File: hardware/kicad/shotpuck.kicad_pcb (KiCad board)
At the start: 2 copper layers, 36 x 34.8 mm, 34 parts, among them J1 Samzo PR5L4015-2P-C-F, J2 SWD pads, Q1 DMN63D8LDW, Q2 DMN2004DWK, U1 BMD-340-A-R, U2 LSM6DSO32TR, U3 MCP73831T-2ACI/OT, U4 BQ29700DSER

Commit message: Refine ShotPuck design with updated component specifications and enhanced documentation
- Updated `README.md` to clarify new component specifications and assembly instructions.
- Revised `VALIDATION.md` to include updated performance metrics and validation steps.
- Adjusted `design.py` to reflect changes in component layout and configurations.
- Enhanced `gen_bom.py` and `gen_jlc.py` to ensure accurate sourcing of components.
- Improved `layout.json` to accommodate new design parameters and dimensions.

Co-Authored-By: Claude Opus 5.5 <noreply@anthropic.com>
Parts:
- moved J2 1.12 mm to (-1.70, -13.5)
- moved U1 1.12 mm to (0.00, -11.0)
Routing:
- net GND: track 131.6 -> 66.2 mm, vias 37 -> 35
- net CHG_INH: track 16.4 -> 20.3 mm
- net VBAT: track 39.4 -> 36.0 mm
- net VIN: track 68.4 -> 70.1 mm
- net SCL: track 4.75 -> 3.54 mm
- net ACC_INT1: track 6.94 -> 5.75 mm
- net SDA: track 4.36 -> 3.34 mm
- net VBUS_SNS: track 10.1 -> 11.0 mm
- net VDD: track 24.0 -> 23.2 mm
- net LED_IO: track 1.68 -> 2.29 mm

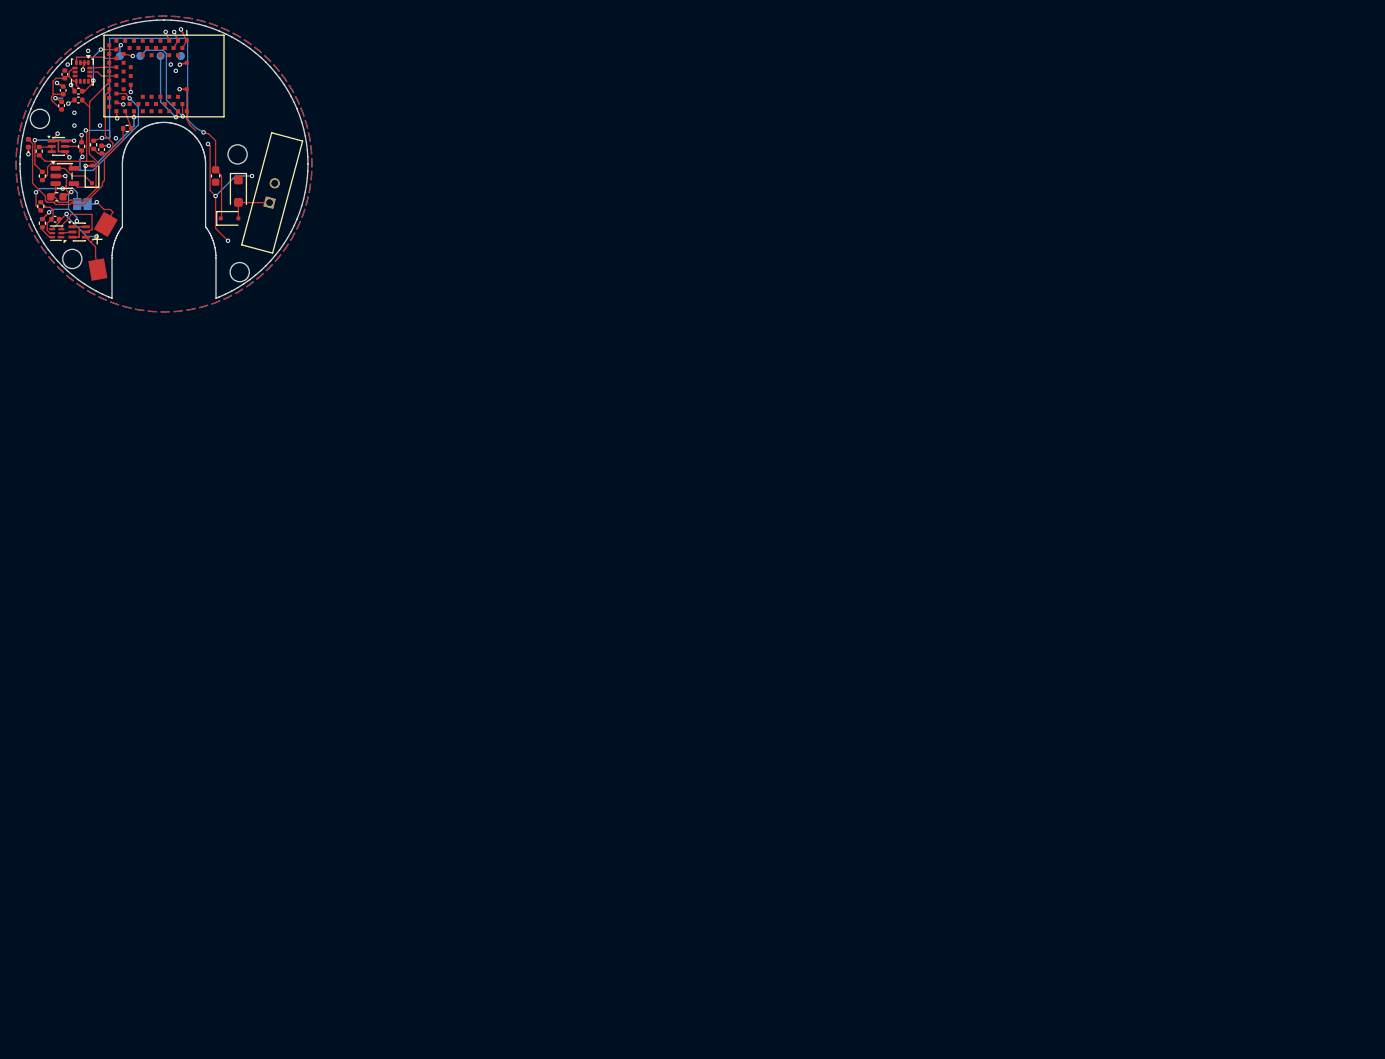
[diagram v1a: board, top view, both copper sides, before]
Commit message: Add USB-C side-port board variant
- J1: side-mounted HRO TYPE-C-31-M-17 (6-pin, power only) replaces the
  magnetic Samzo connector; R10/R11 5.1k pull CC1/CC2 down. Footprint copy
  ShotPuck:..._NoFrontSilk drops the silkscreen outside the board edge.
- Module slid 45 deg around the sleeve; copper-free right side
  (board_shape.rf_keepout), IMU and its caps moved next to the module.
- Decoupling: C5 removed from board and schematic (the BMD-340 has 4.7 uF
  on VCC inside, C4 stays); C6/C7 moved next to IMU pins 8 and 5, C1 next
  to the charger input, vias moved out of U3's pads.
- BT1 uses ShotPuck:LIR1254_Contacts_Edit (pad 2 at 270 deg).
- Schematic: local power symbol ShotPuck:GND_LOCAL keeps the net /GND.
- DRC with zone refill: 0 errors, 0 unconnected, schematic parity clean.

design.py, gen_sch.py and gen_pcb.py still list C5, and gen_sch.py
rewrites ShotPuck.kicad_sym without GND_LOCAL: regenerating undoes the
hand edits.

Co-Authored-By: Claude Opus 5.5 <noreply@anthropic.com>
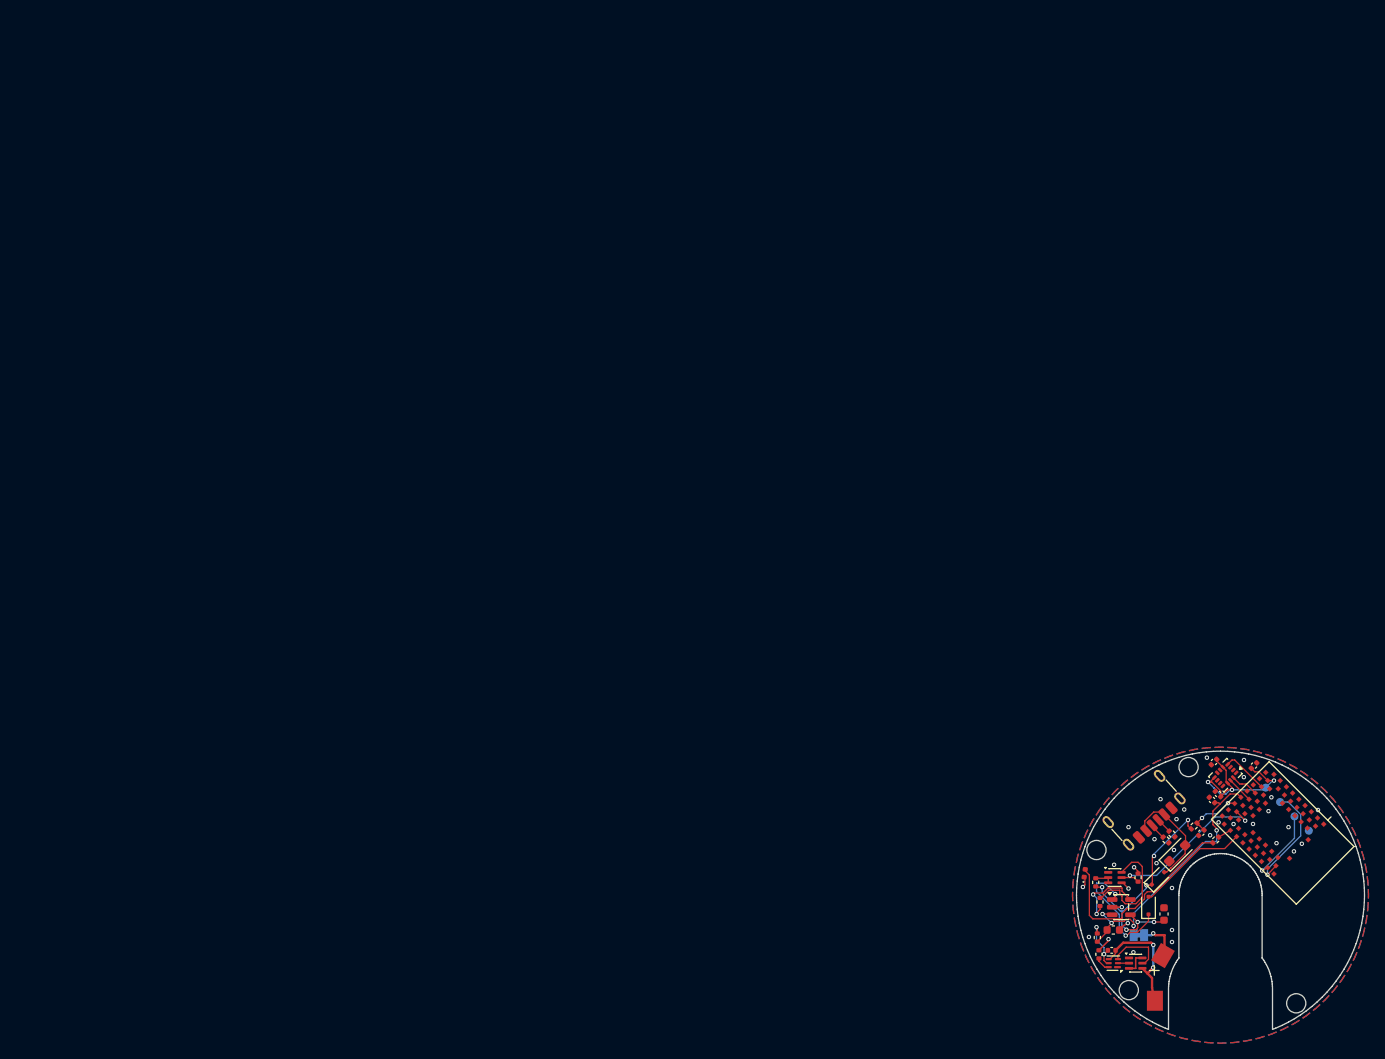
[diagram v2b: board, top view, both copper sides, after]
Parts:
- removed C5: 100n, Capacitor_SMD:C_0402_1005Metric
- added R10: 5.1k 1%, Resistor_SMD:R_0402_1005Metric, F.Cu at (126.0, 83.8)
- added R11: 5.1k 1%, Resistor_SMD:R_0402_1005Metric, F.Cu at (125.2, 84.5)
- BT1: footprint ShotPuck:LIR1254_Contacts -> ShotPuck:LIR1254_Contacts_Edit
- J1: value Samzo PR5L4015-2P-C-F -> TYPE-C-31-M-17; footprint ShotPuck:MagPogo_Samzo_2P -> ShotPuck:USB_C_Receptacle_HRO_TYPE-C-31-M-17_NoFrontSilk
- moved J2 170.5 mm to (140.4, 80.6), turned to -45 degrees
- moved C4 170.4 mm to (136.2, 75.2), turned to 45 degrees
- moved C6 169.9 mm to (131.8, 78.8), turned to 135 degrees
- moved U1 168.8 mm to (139.8, 83.6), turned to 135 degrees
- moved U2 167.7 mm to (132.7, 76.4), turned to -135 degrees
- moved C7 166.6 mm to (131.2, 74.8), turned to -135 degrees
- moved C3 166.5 mm to (131.0, 79.5), turned to 135 degrees
- moved R4 162.6 mm to (131.5, 84.5), turned to -135 degrees
- moved C9 161.8 mm to (129.7, 83.6), turned to -135 degrees
- moved R9 161.8 mm to (128.8, 82.8), turned to 45 degrees
- moved C2 160.7 mm to (118.7, 95.8)
- moved BT1 160.7 mm to (132.1, 103.1)
- moved H2 160.6 mm to (116.6, 85.8)
- moved Q2 160.6 mm to (121.5, 99.9)
- moved R3 160.6 mm to (121.8, 89.2)
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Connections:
- net ACC_INT1 renamed /ACC_INT1
- net BAT_N renamed /BAT_N
- net BAT_P renamed /BAT_P
- net CHG_INH renamed /CHG_INH
- net CHG_STAT renamed /CHG_STAT
- net LED_A renamed /LED_A
- net LED_IO renamed /LED_IO
- net PCM_BAT renamed /PCM_BAT
- net PCM_COUT renamed /PCM_COUT
- net PCM_D renamed /PCM_D
- net PCM_DOUT renamed /PCM_DOUT
- net PCM_VM renamed /PCM_VM
- net PROG renamed /PROG
- net PROG_SW renamed /PROG_SW
- net Q1_GATE renamed /Q1_GATE
- net SCL renamed /SCL
- net SDA renamed /SDA
- net STAT renamed /STAT
- net SWDCLK renamed /SWDCLK
- net SWDIO renamed /SWDIO
- net VBAT renamed /VBAT
- net VBUS_SNS renamed /VBUS_SNS
- net VDD renamed /VDD
- net VIN renamed /VIN
- C1 pad 2: GND -> /GND
- C2 pad 2: GND -> /GND
- C3 pad 2: GND -> /GND
- C4 pad 2: GND -> /GND
- C6 pad 2: GND -> /GND
- C7 pad 2: GND -> /GND
- C9 pad 2: GND -> /GND
- D1 pad 2: VIN_RAW -> /VIN_RAW
- D3 pad 1: GND -> /GND
- D3 pad 2: VIN_RAW -> /VIN_RAW
- D4 pad 1: GND -> /GND
- J2 pad 4: GND -> /GND
- Q1 pad 1: GND -> /GND
- Q1 pad 4: GND -> /GND
- Q2 pad 1: GND -> /GND
- R3 pad 2: GND -> /GND
- R8 pad 2: GND -> /GND
- U1 pad 1: GND -> /GND
- U1 pad 10: (no net) -> unconnected-(U1-P0.29-Pad10)
- U1 pad 11: (no net) -> unconnected-(U1-P0.30-Pad11)
- U1 pad 12: (no net) -> unconnected-(U1-P0.31-Pad12)
- U1 pad 13: (no net) -> unconnected-(U1-P0.00-Pad13)
- U1 pad 14: (no net) -> unconnected-(U1-P0.01-Pad14)
- U1 pad 15: (no net) -> unconnected-(U1-P0.02-Pad15)
- U1 pad 16: GND -> /GND
- U1 pad 18: GND -> /GND
- U1 pad 2: GND -> /GND
- U1 pad 20: (no net) -> unconnected-(U1-P0.04-Pad20)
- U1 pad 22: (no net) -> unconnected-(U1-P0.06-Pad22)
- U1 pad 24: (no net) -> unconnected-(U1-P0.08-Pad24)
- U1 pad 25: (no net) -> unconnected-(U1-P0.09-Pad25)
- U1 pad 26: (no net) -> unconnected-(U1-P0.10-Pad26)
- U1 pad 28: (no net) -> unconnected-(U1-P0.12-Pad28)
- U1 pad 29: GND -> /GND
- U1 pad 3: GND -> /GND
- U1 pad 30: GND -> /GND
- U1 pad 32: (no net) -> unconnected-(U1-P0.14-Pad32)
- U1 pad 34: (no net) -> unconnected-(U1-P0.16-Pad34)
- U1 pad 35: (no net) -> unconnected-(U1-P0.17-Pad35)
- U1 pad 36: (no net) -> unconnected-(U1-P0.21-Pad36)
- U1 pad 37: (no net) -> unconnected-(U1-P0.19-Pad37)
- U1 pad 38: (no net) -> unconnected-(U1-P0.20-Pad38)
- U1 pad 39: (no net) -> unconnected-(U1-P0.18-Pad39)
- U1 pad 4: GND -> /GND
- U1 pad 40: (no net) -> unconnected-(U1-P0.22-Pad40)
- U1 pad 41: (no net) -> unconnected-(U1-P0.23-Pad41)
- U1 pad 42: (no net) -> unconnected-(U1-P0.24-Pad42)
- U1 pad 45: GND -> /GND
- U1 pad 46: GND -> /GND
- U1 pad 47: GND -> /GND
- U1 pad 48: (no net) -> unconnected-(U1-P1.05-Pad48)
- U1 pad 49: (no net) -> unconnected-(U1-P1.06-Pad49)
- U1 pad 5: GND -> /GND
- U1 pad 50: (no net) -> unconnected-(U1-P1.07-Pad50)
- U1 pad 51: (no net) -> unconnected-(U1-P1.08-Pad51)
- U1 pad 52: (no net) -> unconnected-(U1-P1.09-Pad52)
- U1 pad 53: (no net) -> unconnected-(U1-P1.10-Pad53)
- U1 pad 54: (no net) -> unconnected-(U1-P1.11-Pad54)
- U1 pad 55: GND -> /GND
- U1 pad 56: (no net) -> unconnected-(U1-P1.00-Pad56)
- U1 pad 57: (no net) -> unconnected-(U1-P1.01-Pad57)
- U1 pad 58: (no net) -> unconnected-(U1-P1.02-Pad58)
- U1 pad 59: (no net) -> unconnected-(U1-P1.03-Pad59)
- U1 pad 6: (no net) -> unconnected-(U1-P0.25-Pad6)
- U1 pad 60: (no net) -> unconnected-(U1-P1.04-Pad60)
- U1 pad 61: (no net) -> unconnected-(U1-P1.12-Pad61)
- U1 pad 62: (no net) -> unconnected-(U1-P1.13-Pad62)
- U1 pad 63: (no net) -> unconnected-(U1-P1.14-Pad63)
- U1 pad 64: (no net) -> unconnected-(U1-P1.15-Pad64)
- U1 pad 67: (no net) -> unconnected-(U1-USB-D--Pad67)
- U1 pad 68: (no net) -> unconnected-(U1-USB-D+-Pad68)
- U1 pad 7: (no net) -> unconnected-(U1-P0.26-Pad7)
- U1 pad 8: (no net) -> unconnected-(U1-P0.27-Pad8)
- U1 pad 9: (no net) -> unconnected-(U1-P0.28-Pad9)
- U2 pad 1: GND -> /GND
- U2 pad 10: (no net) -> unconnected-(U2-NC-Pad10)
- U2 pad 11: (no net) -> unconnected-(U2-NC-Pad11)
- U2 pad 2: GND -> /GND
- U2 pad 3: GND -> /GND
- U2 pad 6: GND -> /GND
- U2 pad 7: GND -> /GND
- U2 pad 9: (no net) -> unconnected-(U2-INT2-Pad9)
- U3 pad 2: GND -> /GND
- U4 pad 1: (no net) -> unconnected-(U4-NC-Pad1)
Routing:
- net GND: track 66.2 -> 0.00 mm, vias 35 -> 0
- net /VIN: track 70.1 -> 31.0 mm, vias 3 -> 7
- net /VIN_RAW: track 0.00 -> 14.0 mm
- net /STAT: track 5.30 -> 16.3 mm, vias 0 -> 2
- net /GND: track 0.00 -> 7.91 mm, vias 0 -> 33
- net VIN_RAW: track 5.91 -> 0.00 mm
- net /PROG: track 5.57 -> 9.30 mm, vias 0 -> 2
- net /VBUS_SNS: track 11.0 -> 7.42 mm, vias 0 -> 2
- net /PROG_SW: track 11.5 -> 14.5 mm, vias 2 -> 0
- net /CHG_STAT: track 11.5 -> 13.8 mm, vias 2 -> 0
- net /CC1: track 0.00 -> 2.09 mm
- net /CC2: track 0.00 -> 2.05 mm
- net /BAT_N: track 13.5 -> 15.2 mm
- net /CHG_INH: track 20.3 -> 21.8 mm
- net /PCM_BAT: track 5.54 -> 6.79 mm, vias 0 -> 2
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- added copper zone on B.Cu, net /GND
- added copper zone on F.Cu, net /GND
- removed copper zone on B.Cu, net GND
- removed copper zone on F.Cu, net GND

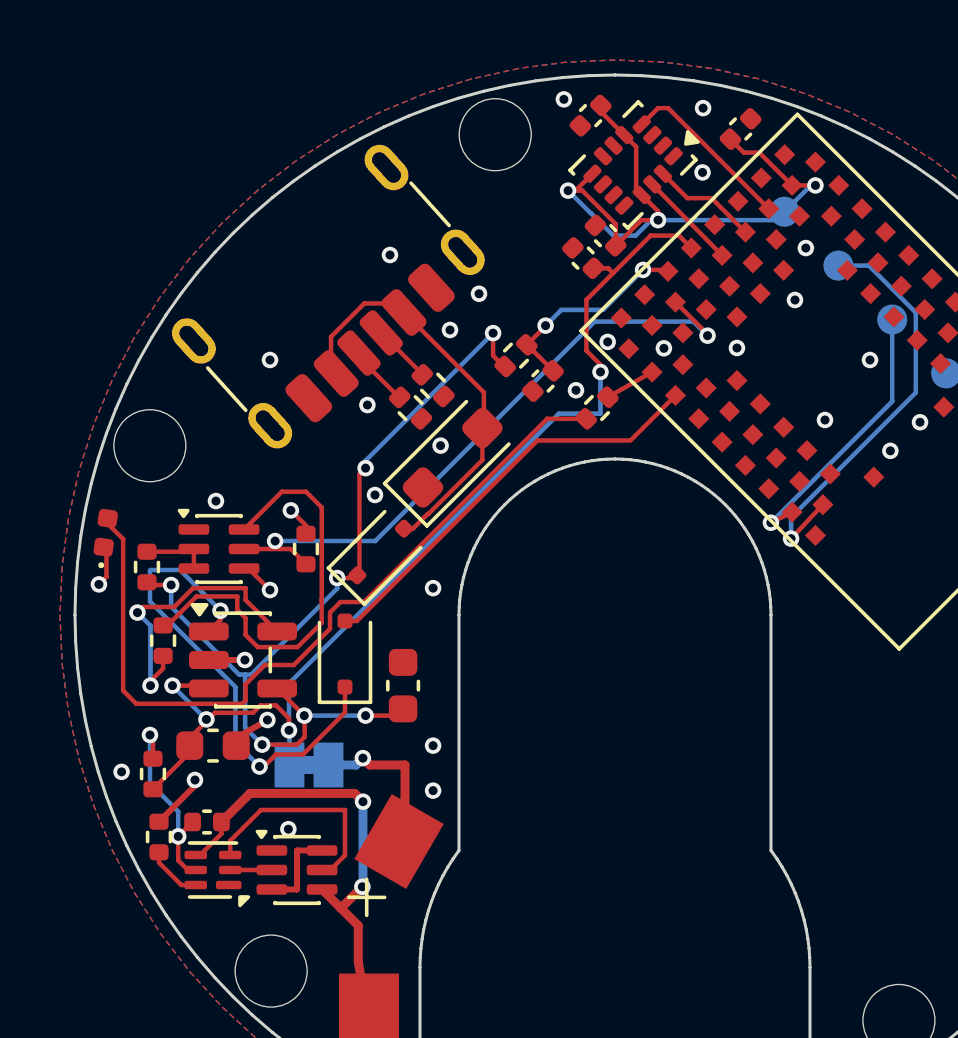
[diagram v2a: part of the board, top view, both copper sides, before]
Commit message: Switch J1 to waterproof IPX8 USB-C (C3020041) and seal the cap
- J1: SHOU HAN TYPE-C 6PFS 2JCB1.6-H6.7 IPX8 (LCSC C3020041), recessed
  into a 10.28 x 5.22 mm notch in the board edge at 132.58 deg, midway
  between H1 and H2. Footprint from the datasheet drawing (pads kept
  0.3/0.35 mm from the notch; the notch sides run through two 0.70 mm
  NPTH holes for the legs, since the datasheet's 0.69 mm U-slots cannot
  be routed); LCSC's STEP model shifted -1.93 mm onto the pads.
- H1/H2 moved apart so the ground pour reaches the wing tabs; layout.json
  bosses follow (plate holes, cap bosses, standoffs).
- GND via at (-0.41, 16.09): the pour around U2's GND pins 6/7 reached
  the rest of GND only along the rim, where the top tab's mouse bites cut
  it.
- Cap: the silicone ring seals in an obround hole in the wall (0.15 mm
  squeeze per side), a flat at the receptacle face lets any compliant
  plug seat fully, a pocket over the body leaves 0.67 mm of cap top.
  CadQuery check with the real STEP model: only the ring squeeze
  overlaps; a maximum-size plug overmold clears cap and plate.
- Panel: 2 mm backbone between the rows, top tab 1.5 mm wide at 86 deg
  (clear of H1 and the via at 80 deg); panel 91.1 x 92.7 mm.
- gen_panel.py places tabs from the board's own centre (the board sits at
  (132.06, 91.40) on the KiCad page); the Blender GLB export uses the
  same origin and takes J1 from the board.
- Board DRC 0/0 with schematic parity; panel DRC 0/0; BOM/CPL/Gerbers
  regenerated.

mechanical/out/shotpuck_assembly.mp4 and .blend are from the render
before the waterproof port and still show the earlier cap; re-render
with mechanical/blender/render_assembly.py. gen_pcb.py does not draw
the port notch, and design.py still lists C5.

Co-Authored-By: Claude Opus 5.5 <noreply@anthropic.com>
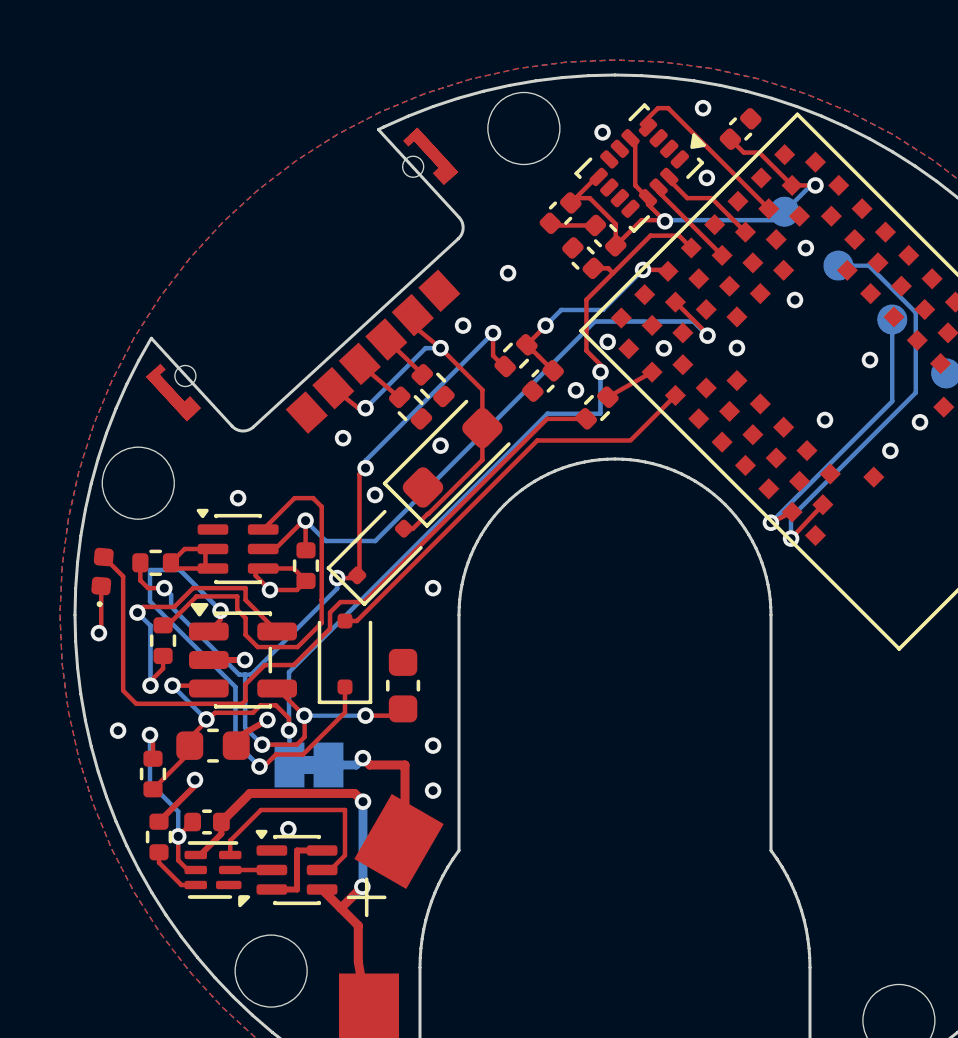
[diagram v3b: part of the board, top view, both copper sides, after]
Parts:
- J1: value TYPE-C-31-M-17 -> TYPE-C 6PFS 2JCB1.6-H6.7 IPX8; footprint ShotPuck:USB_C_Receptacle_HRO_TYPE-C-31-M-17_NoFrontSilk -> ShotPuck:USB_C_Receptacle_ShouHan_TYPE-C-6PFS-2JCB1.6-H6.7_IPX8
- moved C7 3.40 mm to (130.2, 78.0)
- moved J1 1.57 mm to (122.7, 81.2), turned to -137.424 degrees
- moved H2 1.31 mm to (116.2, 87.0)
- moved D4 1.30 mm to (115.0, 89.9), turned to 85 degrees
- moved H1 0.98 mm to (129.0, 75.2)
- moved Q1 0.64 mm to (119.5, 89.2)
- moved R3 0.55 mm to (121.8, 89.8), turned to -90 degrees
- moved R2 0.32 mm to (116.8, 89.7), turned to 0 degrees
- moved U2 0.23 mm to (132.9, 76.5)
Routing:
- net /VDD: track 24.1 -> 18.3 mm, vias 3 -> 2
- net /GND: track 7.91 -> 11.4 mm, vias 33 -> 30
- net /LED_A: track 26.1 -> 24.9 mm
- net /Q1_GATE: track 2.35 -> 3.35 mm
- net /PROG_SW: track 14.5 -> 13.7 mm
- net /VIN: track 31.0 -> 31.6 mm
- net /VIN_RAW: track 14.0 -> 14.2 mm, vias 0 -> 2
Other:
- outline, holes or cut-outs redrawn
